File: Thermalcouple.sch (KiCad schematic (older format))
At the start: 0 parts

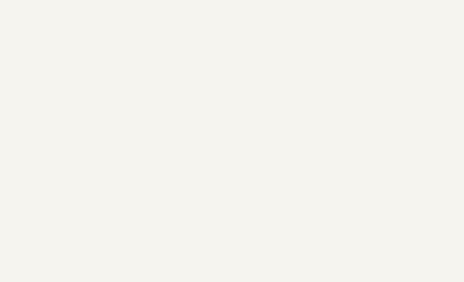
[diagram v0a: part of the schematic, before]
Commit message: Definging inputs and outputs
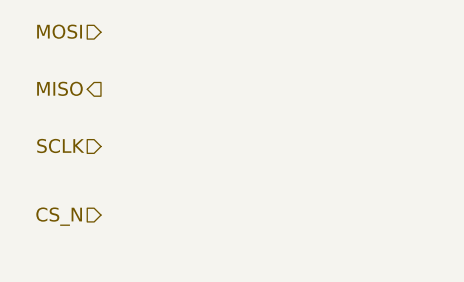
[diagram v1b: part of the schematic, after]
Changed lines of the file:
@@
 LIBS:contrib
 LIBS:valves
+LIBS:BenchBuddy-cache
 EELAYER 27 0
 EELAYER END
@@
 Sheet 3 8
 Title ""
-Date "2 feb 2014"
+Date "3 feb 2014"
 Rev ""
 Comp ""
@@
 Text HLabel 8650 2950 2    60   Input ~ 0
 TC IN -
+Text HLabel 2500 2000 0    60   Input ~ 0
+MOSI
+Text HLabel 2500 2250 0    60   Output ~ 0
+MISO
+Text HLabel 2500 2500 0    60   Input ~ 0
+SCLK
+Text HLabel 2500 2800 0    60   Input ~ 0
+CS_N
 $EndSCHEMATC

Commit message: Thermal Couple placeholder
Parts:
- added D?: ZENER, ~, symbol ZENER
- added R? (x7): R, ~, symbol R
- added U? (x4): LM324, symbol LM324
- added U? (x2): MCP3550-50-E/MS, MSOP-8, symbol MCP3550-50-E/MS
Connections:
- net CS_N: now also U?.7 (~CS~)
- net MISO: now also U?.6 (SDO/~RDY~)
- net SCLK: now also U?.5 (SCK)
- net TC IN +: now also U?.3 (+)
- net TC IN -: now also U?.3 (+)
- new net: R?.1, R?.2, U?.1
- new net: R?.1, R?.2, U?.2 (-) (x3)
- new net: R?.2, R?.2, U?.1
- new net: R?.1, U?.1
- new net: R?.1, R?.2, U?.3 (+)
- new net: U?.1, U?.2 (-), U?.2 (Vin+)
- new net +12V: U?.4 (V+), U?.4 (V+), U?.4 (V+)
- new net -12V: D?.2 (K), U?.11 (V-), U?.11 (V-), U?.11 (V-), U?.3 (+)
- new net AGND: D?.1 (A), R?.1, U?.3 (Vin-), U?.3 (Vin-)
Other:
- note added: "16-24bit ADC"
- note added: "Analog/TC"
- note added: "General Temperature Sensor (placeholder)\n"
- note added: "Instrumental Amp"
